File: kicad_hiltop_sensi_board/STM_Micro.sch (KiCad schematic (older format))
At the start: 20 parts, among them SW1 SW_Push, U22 STM32F072RBTx, Y2 8MHZ, Y3 ABS25-32.768KHZ-6-T

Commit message: Updated sensi board pin map and layout before PCB tracking
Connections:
- net ADC10: now also U22.10 (PC2/ADC_IN12/I2S2_MCK/SPI2_MISO); no longer U22.25 (PC5/ADC_IN15/SYS_WKUP5/TSC_G3_IO1/USART3_RX)
- net ADC11: now also U22.11 (PC3/ADC_IN13/I2S2_SD/SPI2_MOSI); no longer U22.24 (PC4/ADC_IN14/USART3_TX)
- net ADC12: now also U22.24 (PC4/ADC_IN14/USART3_TX); no longer U22.23 (ADC_IN7/COMP2_OUT/I2S1_SD/SPI1_MOSI/TIM14_CH1/TIM17_CH1/TIM1_CH1N/TIM3_CH2/TSC_G2_IO4/PA7)
- net ADC13: now also U22.25 (PC5/ADC_IN15/SYS_WKUP5/TSC_G3_IO1/USART3_RX); no longer U22.8 (PC0/ADC_IN10)
- net ADC2: now also U22.16 (ADC_IN2/COMP2_INM/COMP2_OUT/SYS_WKUP4/TIM15_CH1/TIM2_CH3/TSC_G1_IO3/USART2_TX/PA2); no longer U22.11 (PC3/ADC_IN13/I2S2_SD/SPI2_MOSI)
- net ADC3: now also U22.17 (ADC_IN3/COMP2_INP/TIM15_CH2/TIM2_CH4/TSC_G1_IO4/USART2_RX/PA3); no longer U22.10 (PC2/ADC_IN12/I2S2_MCK/SPI2_MISO)
- net ADC4: now also U22.20 (ADC_IN4/COMP1_INM/COMP2_INM/DAC_OUT1/I2S1_WS/SPI1_NSS/TIM14_CH1/TSC_G2_IO1/USART2_CK/PA4); no longer U22.9 (PC1/ADC_IN11)
- net ADC5: now also U22.22 (ADC_IN6/COMP1_OUT/I2S1_MCK/SPI1_MISO/TIM16_CH1/TIM1_BKIN/TIM3_CH1/TSC_G2_IO3/USART3_CTS/PA6); no longer U22.16 (ADC_IN2/COMP2_INM/COMP2_OUT/SYS_WKUP4/TIM15_CH1/TIM2_CH3/TSC_G1_IO3/USART2_TX/PA2)
- net ADC6: now also U22.23 (ADC_IN7/COMP2_OUT/I2S1_SD/SPI1_MOSI/TIM14_CH1/TIM17_CH1/TIM1_CH1N/TIM3_CH2/TSC_G2_IO4/PA7); no longer U22.17 (ADC_IN3/COMP2_INP/TIM15_CH2/TIM2_CH4/TSC_G1_IO4/USART2_RX/PA3)
- net ADC7: now also U22.27 (ADC_IN9/TIM14_CH1/TIM1_CH3N/TIM3_CH4/TSC_G3_IO3/USART3_DE/USART3_RTS/PB1); no longer U22.20 (ADC_IN4/COMP1_INM/COMP2_INM/DAC_OUT1/I2S1_WS/SPI1_NSS/TIM14_CH1/TSC_G2_IO1/USART2_CK/PA4)
- net ADC8: now also U22.8 (PC0/ADC_IN10); no longer U22.22 (ADC_IN6/COMP1_OUT/I2S1_MCK/SPI1_MISO/TIM16_CH1/TIM1_BKIN/TIM3_CH1/TSC_G2_IO3/USART3_CTS/PA6)
- net ADC9: now also U22.9 (PC1/ADC_IN11); no longer U22.27 (ADC_IN9/TIM14_CH1/TIM1_CH3N/TIM3_CH4/TSC_G3_IO3/USART3_DE/USART3_RTS/PB1)
- net DUT1_UART_RX_GPIO15: now also U22.51 (PC10/USART3_TX/USART4_TX); no longer U22.52 (PC11/USART3_RX/USART4_RX)
- net DUT1_UART_TX_GPIO16: now also U22.52 (PC11/USART3_RX/USART4_RX); no longer U22.53 (PC12/USART3_CK/USART4_CK)
- net GPIO13: now also U22.26 (ADC_IN8/TIM1_CH2N/TIM3_CH3/TSC_G3_IO2/USART3_CK/PB0); no longer U22.40 (PC9/DAC_EXTI9/TIM3_CH4)
- net GPIO14: now also U22.28 (TSC_G3_IO4/PB2); no longer U22.26 (ADC_IN8/TIM1_CH2N/TIM3_CH3/TSC_G3_IO2/USART3_CK/PB0)
- net GPIO3: now also U22.40 (PC9/DAC_EXTI9/TIM3_CH4); no longer U22.28 (TSC_G3_IO4/PB2)
- net at R121.2: now also U22.53 (PC12/USART3_CK/USART4_CK); no longer U22.51 (PC10/USART3_TX/USART4_TX)
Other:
- moved on the sheet: R121
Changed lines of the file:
@@
 Text HLabel 11775 5775 2    60   Output ~ 0
 DEBUG_UART_TX
-Text HLabel 3925 4975 0    60   Input ~ 0
+Text HLabel 11800 3375 2    60   Input ~ 0
 ADC3
 $Comp
@@
 Text HLabel 11800 3875 2    60   BiDi ~ 0
 GPIO2
-Text HLabel 11800 3475 2    60   Input ~ 0
-ADC7
-Text HLabel 4400 5675 0    60   BiDi ~ 0
+Text HLabel 11800 4775 2    60   BiDi ~ 0
 GPIO13
 Text HLabel 11775 5575 2    60   BiDi ~ 0
@@
 Text HLabel 4400 6075 0    60   BiDi ~ 0
 GPIO11
-Text HLabel 11800 4775 2    60   BiDi ~ 0
+Text HLabel 11800 4975 2    60   BiDi ~ 0
 GPIO14
 Text HLabel 11775 6275 2    60   BiDi ~ 0
 GPIO7
-Text HLabel 11800 3775 2    60   Input ~ 0
+Text HLabel 3925 5175 0    60   Input ~ 0
 ADC12
-Text HLabel 3925 4775 0    60   Input ~ 0
+Text HLabel 3925 5275 0    60   Input ~ 0
 ADC13
 Text HLabel 11800 3175 2    60   BiDi ~ 0
@@
 Text HLabel 11775 5675 2    60   Output ~ 0
 RL1
-Text HLabel 2500 5875 0    60   BiDi ~ 0
+Text HLabel 2500 5775 0    60   BiDi ~ 0
 DUT1_UART_RX_GPIO15
 Text HLabel 3925 5575 0    60   Input ~ 0
 GPIO1
-Text HLabel 11800 3375 2    60   Input ~ 0
-ADC6
 Wire Wire Line
 	10400 5075 11800 5075
@@
 Wire Wire Line
 	10400 3175 11800 3175
-Text HLabel 2500 5975 0    60   BiDi ~ 0
+Text HLabel 2500 5875 0    60   BiDi ~ 0
 DUT1_UART_TX_GPIO16
 Text HLabel 3925 5475 0    60   BiDi ~ 0
@@
 Text HLabel 11800 4475 2    60   Input ~ 0
 SWD_SCK
-Text HLabel 11800 4875 2    60   Input ~ 0
+Text HLabel 3925 4875 0    60   Input ~ 0
 ADC9
-Text HLabel 11800 3675 2    60   Input ~ 0
+Text HLabel 3925 4775 0    60   Input ~ 0
 ADC8
-Text HLabel 3925 4875 0    60   Input ~ 0
+Text HLabel 11800 3475 2    60   Input ~ 0
 ADC4
 Text HLabel 11800 3275 2    60   Input ~ 0
-ADC5
-Text HLabel 3925 5075 0    60   Input ~ 0
 ADC2
 Text HLabel 11800 3075 2    60   Input ~ 0
@@
 Text HLabel 11800 5975 2    60   Output ~ 0
 HS_OUT2
-Text HLabel 11800 4975 2    60   BiDi ~ 0
+Text HLabel 4400 5675 0    60   BiDi ~ 0
 GPIO3
 Text HLabel 11775 6175 2    60   BiDi ~ 0
 GPIO6
 Wire Wire Line
-	3800 5775 4400 5775
+	3800 5975 4400 5975
 Wire Wire Line
-	3500 5775 3025 5775
+	3500 5975 3025 5975
 Text HLabel 11775 5875 2    60   Input ~ 0
 DEBUG_UART_RX
-Text HLabel 3025 5775 0    60   Output ~ 0
+Text HLabel 3025 5975 0    60   Output ~ 0
 HS_OUT3
 $Comp
 L Sensi_Board-rescue:R-device R121
 U 1 1 5FA9D488
-P 3650 5775
-F 0 "R121" V 3625 5550 50  0000 C CNN
-F 1 "0R" V 3625 5975 50  0000 C CNN
-F 2 "Resistor_SMD:R_0603_1608Metric" V 3580 5775 50  0001 C CNN
-F 3 "" H 3650 5775 50  0001 C CNN
-F 4 "101-005" H -7275 1400 50  0001 C CNN "Devtank"
-	1    3650 5775
+P 3650 5975
+F 0 "R121" V 3625 5750 50  0000 C CNN
+F 1 "0R" V 3625 6175 50  0000 C CNN
+F 2 "Resistor_SMD:R_0603_1608Metric" V 3580 5975 50  0001 C CNN
+F 3 "" H 3650 5975 50  0001 C CNN
+F 4 "101-005" H -7275 1600 50  0001 C CNN "Devtank"
+	1    3650 5975
 	0    -1   1    0
 $EndComp
 Wire Wire Line
-	2500 5875 4400 5875
+	2500 5775 4400 5775
 Wire Wire Line
-	4400 5975 2500 5975
+	4400 5875 2500 5875
 Wire Wire Line
 	10400 5975 11800 5975
-Text HLabel 3925 5275 0    60   Input ~ 0
+Text HLabel 3925 4975 0    60   Input ~ 0
 ADC10
-Text HLabel 3925 5175 0    60   Input ~ 0
+Text HLabel 3925 5075 0    60   Input ~ 0
 ADC11
 Wire Wire Line
 	7500 1725 7500 1825
+Text HLabel 11800 3675 2    60   Input ~ 0
+ADC5
+Text HLabel 11800 3775 2    60   Input ~ 0
+ADC6
+Text HLabel 11775 4875 2    60   Input ~ 0
+ADC7
 $EndSCHEMATC

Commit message: Most major connections complete and differential tracking done on the Sensi board layout
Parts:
- removed R121: 0R, Resistor_SMD:R_0603_1608Metric, symbol Sensi_Board-rescue:R-device
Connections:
- net HS_OUT3: now also U22.53 (PC12/USART3_CK/USART4_CK)
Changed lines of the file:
@@
 Connection ~ 7200 1825
 Wire Wire Line
-	7500 2025 7875 2025
+	7500 2025 7750 2025
 Wire Wire Line
 	2125 1275 2125 1375
@@
 Text HLabel 11775 6175 2    60   BiDi ~ 0
 GPIO6
-Wire Wire Line
-	3800 5975 4400 5975
-Wire Wire Line
-	3500 5975 3025 5975
 Text HLabel 11775 5875 2    60   Input ~ 0
 DEBUG_UART_RX
 Text HLabel 3025 5975 0    60   Output ~ 0
 HS_OUT3
-$Comp
-L Sensi_Board-rescue:R-device R121
-U 1 1 5FA9D488
-P 3650 5975
-F 0 "R121" V 3625 5750 50  0000 C CNN
-F 1 "0R" V 3625 6175 50  0000 C CNN
-F 2 "Resistor_SMD:R_0603_1608Metric" V 3580 5975 50  0001 C CNN
-F 3 "" H 3650 5975 50  0001 C CNN
-F 4 "101-005" H -7275 1600 50  0001 C CNN "Devtank"
-	1    3650 5975
-	0    -1   1    0
-$EndComp
 Wire Wire Line
 	2500 5775 4400 5775
@@
 Text HLabel 11775 4875 2    60   Input ~ 0
 ADC7
+$Comp
+L power:PWR_FLAG #FLG0102
+U 1 1 5DAF6A7D
+P 7750 1975
+F 0 "#FLG0102" H 7750 2050 50  0001 C CNN
+F 1 "PWR_FLAG" H 7750 2148 50  0000 C CNN
+F 2 "" H 7750 1975 50  0001 C CNN
+F 3 "" H 7750 1975 50  0001 C CNN
+	1    7750 1975
+	1    0    0    -1
+$EndComp
+Wire Wire Line
+	7750 1975 7750 2025
+Connection ~ 7750 2025
+Wire Wire Line
+	7750 2025 7875 2025
+Wire Wire Line
+	3025 5975 4400 5975
 $EndSCHEMATC

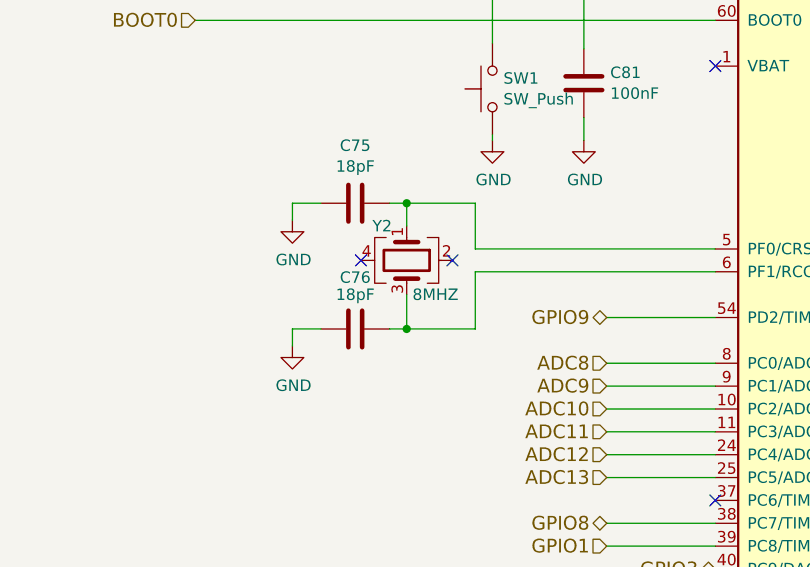
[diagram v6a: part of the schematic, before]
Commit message: Pre stitching via for sensi board.
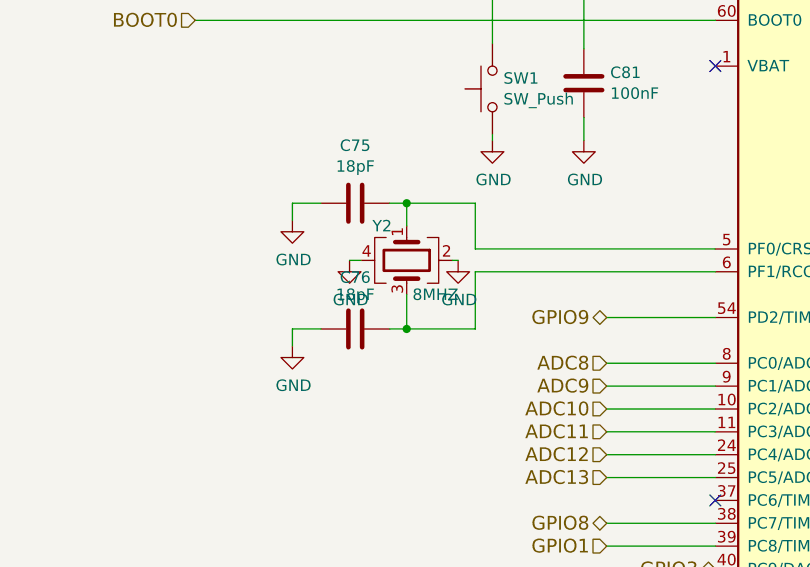
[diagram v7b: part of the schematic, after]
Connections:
- net GND: now also Y2.2, Y2.4
- no-connect marks 6 -> 4
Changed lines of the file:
@@
 NoConn ~ 4400 5375
 NoConn ~ 4400 3475
-NoConn ~ 3250 4325
-NoConn ~ 2850 4325
 NoConn ~ 3425 6550
 NoConn ~ 3025 6550
@@
 Wire Wire Line
 	3025 5975 4400 5975
+$Comp
+L power:GND #PWR0162
+U 1 1 5DB0E805
+P 3275 4325
+F 0 "#PWR0162" H 3275 4075 50  0001 C CNN
+F 1 "GND" H 3280 4152 50  0000 C CNN
+F 2 "" H 3275 4325 50  0001 C CNN
+F 3 "" H 3275 4325 50  0001 C CNN
+	1    3275 4325
+	1    0    0    -1
+$EndComp
+$Comp
+L power:GND #PWR0165
+U 1 1 5DB0F3D3
+P 2800 4325
+F 0 "#PWR0165" H 2800 4075 50  0001 C CNN
+F 1 "GND" H 2805 4152 50  0000 C CNN
+F 2 "" H 2800 4325 50  0001 C CNN
+F 3 "" H 2800 4325 50  0001 C CNN
+	1    2800 4325
+	1    0    0    -1
+$EndComp
+Wire Wire Line
+	2800 4325 2850 4325
+Wire Wire Line
+	3250 4325 3275 4325
 $EndSCHEMATC

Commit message: Sensi board with references visible and without stitching vias
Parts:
- C73, C74, C79, C80: Devtank 105-002 -> 105-019
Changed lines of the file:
@@
 F 2 "Capacitor_SMD:C_0402_1005Metric" H 2163 1475 50  0001 C CNN
 F 3 "" H 2125 1625 50  0001 C CNN
-F 4 "105-002" H 0   0   50  0001 C CNN "Devtank"
+F 4 "105-019" H 0   0   50  0001 C CNN "Devtank"
 	1    2125 1625
 	1    0    0    -1
@@
 F 2 "Capacitor_SMD:C_0402_1005Metric" H 2613 1475 50  0001 C CNN
 F 3 "" H 2575 1625 50  0001 C CNN
-F 4 "105-002" H 0   0   50  0001 C CNN "Devtank"
+F 4 "105-019" H 0   0   50  0001 C CNN "Devtank"
 	1    2575 1625
 	1    0    0    -1
@@
 F 2 "Capacitor_SMD:C_0402_1005Metric" H 3063 1475 50  0001 C CNN
 F 3 "" H 3025 1625 50  0001 C CNN
-F 4 "105-002" H 0   0   50  0001 C CNN "Devtank"
+F 4 "105-019" H 0   0   50  0001 C CNN "Devtank"
 	1    3025 1625
 	1    0    0    -1
@@
 F 2 "Capacitor_SMD:C_0402_1005Metric" H 3513 1475 50  0001 C CNN
 F 3 "" H 3475 1625 50  0001 C CNN
-F 4 "105-002" H 0   0   50  0001 C CNN "Devtank"
+F 4 "105-019" H 0   0   50  0001 C CNN "Devtank"
 	1    3475 1625
 	1    0    0    -1
